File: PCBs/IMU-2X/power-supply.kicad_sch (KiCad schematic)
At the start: 21 parts, among them U3 TPS613222ADBVR, U8 LMR54410FDBVR

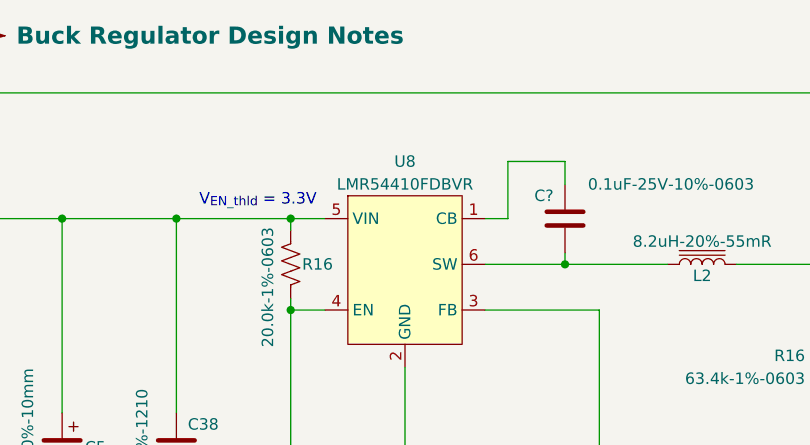
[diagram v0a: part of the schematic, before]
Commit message: Adding IMU-2X-v2 fixes switch footprint.
Signed-off-by: Scott <sgberman1@gmail.com>
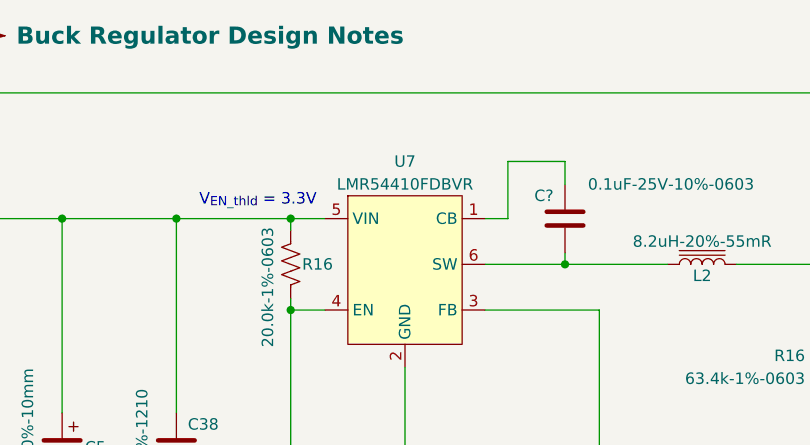
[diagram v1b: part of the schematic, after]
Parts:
- renumbered U8 to U7
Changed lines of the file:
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@@
   (title_block
     (title "IMU-2X")
-    (date "2023-08-12")
-    (rev "1")
+    (date "2023-11-19")
+    (rev "2")
     (company "FRC971 - Spartan Robotics")
   )
@@
       (project "IMU-2X"
         (path "/3a012c22-a9cb-4cb7-8e69-db8529c53ea6/dfddfc9c-e803-47e7-ad6c-6304a5151d35"
-          (reference "C36") (unit 1)
+          (reference "C37") (unit 1)
         )
       )
@@
   (symbol (lib_id "IMU-2X:LMR54410FDBVR") (at 219.71 57.15 0) (unit 1)
     (in_bom yes) (on_board yes) (dnp no)
-    (property "Reference" "U8" (at 226.06 53.34 0)
+    (property "Reference" "U7" (at 226.06 53.34 0)
       (effects (font (size 1.27 1.27)))
     )
@@
       (project "IMU-2X"
         (path "/3a012c22-a9cb-4cb7-8e69-db8529c53ea6/dfddfc9c-e803-47e7-ad6c-6304a5151d35"
-          (reference "U8") (unit 1)
+          (reference "U7") (unit 1)
         )
       )
@@
       (project "IMU-2X"
         (path "/3a012c22-a9cb-4cb7-8e69-db8529c53ea6/dfddfc9c-e803-47e7-ad6c-6304a5151d35"
-          (reference "R15") (unit 1)
-        )
-      )
+          (reference "R13") (unit 1)
+        )
+      )
